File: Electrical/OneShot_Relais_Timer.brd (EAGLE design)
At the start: 65 x 63 mm, 15 parts, among them IC2 ATTINY204SOIC14, K1 RE030012, T1 BC847, X1 MKDSN1,5/3-5,08

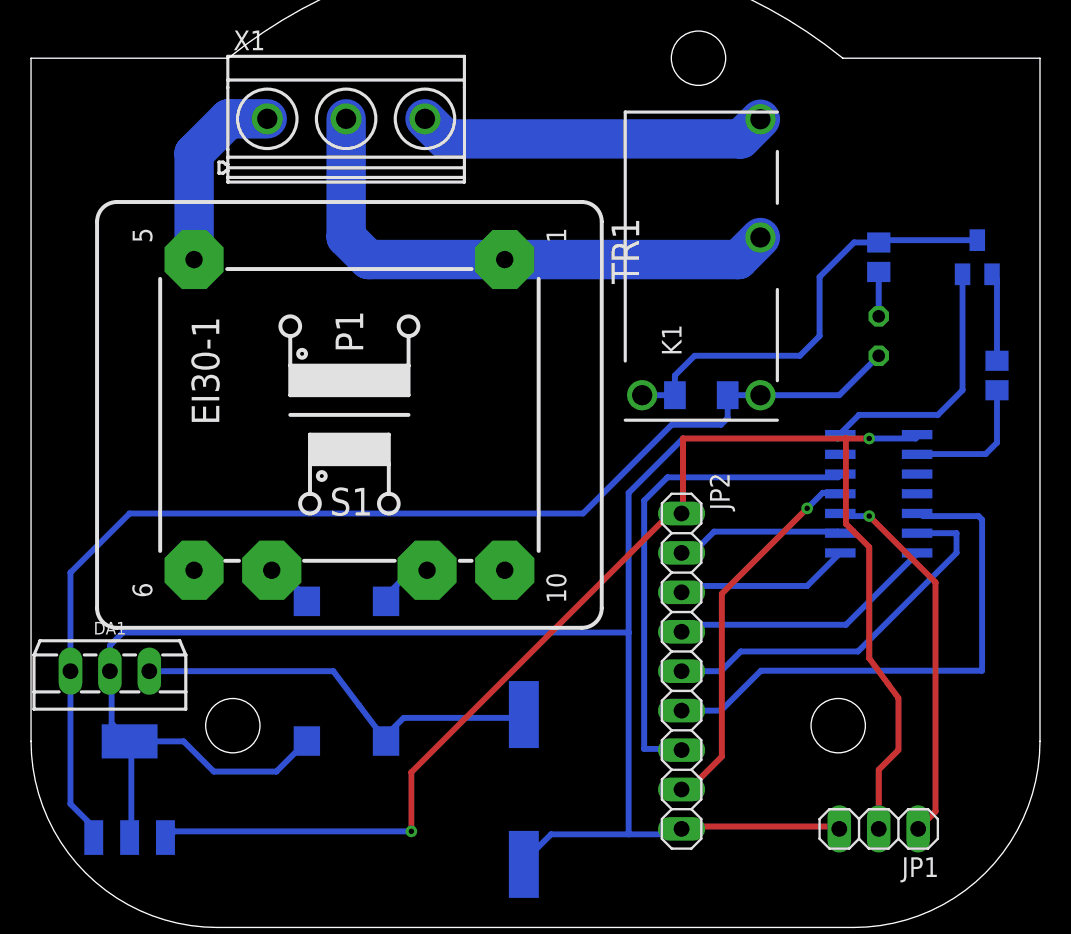
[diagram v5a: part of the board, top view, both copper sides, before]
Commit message: Added mounting hole to PCB
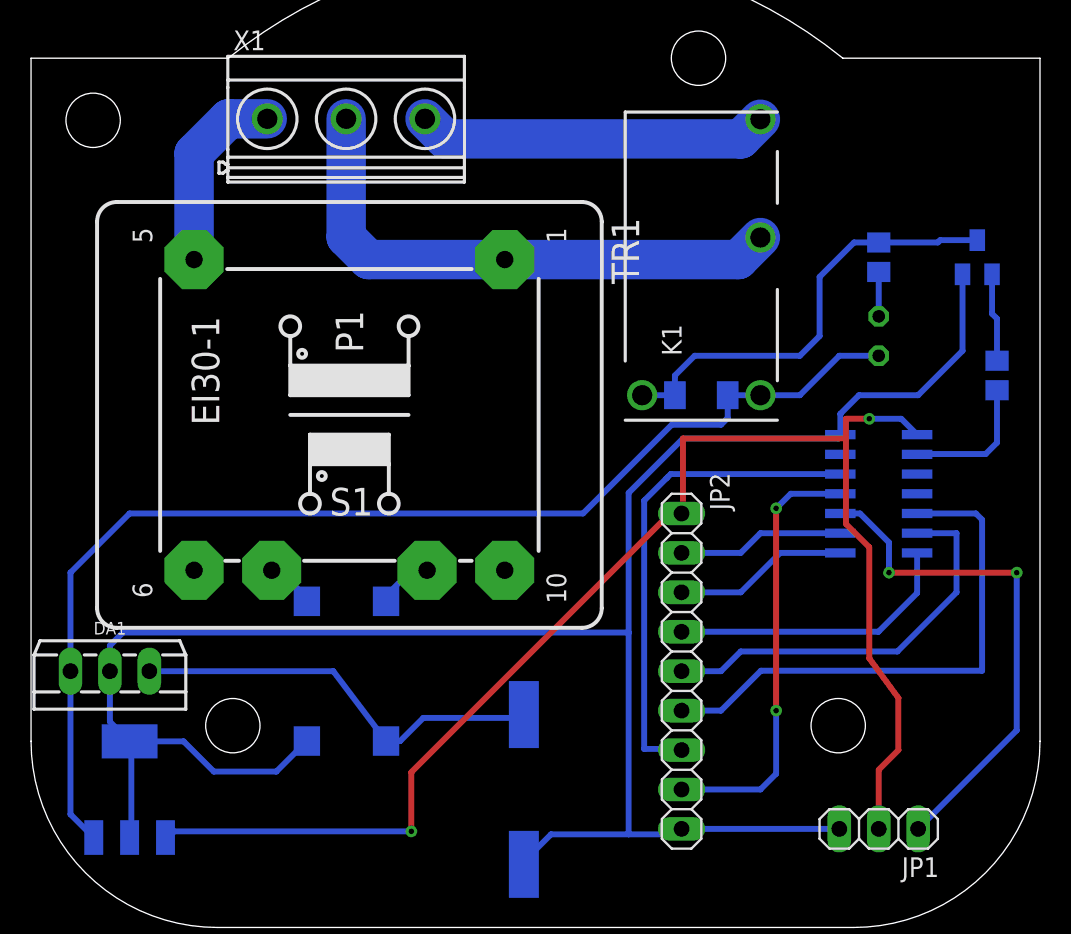
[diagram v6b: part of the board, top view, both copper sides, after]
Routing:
- net N$26: track 24.3 -> 33.2 mm, vias 1 -> 2
- net BTN_SET: track 24.8 -> 28.1 mm, vias 1 -> 2
- net +5V: track 91.1 -> 92.6 mm
- net BCD_7SEG_4: track 24.7 -> 26.2 mm
- net BCD_7SEG_3: track 17.5 -> 18.8 mm
- net GND: track 135.1 -> 134.2 mm

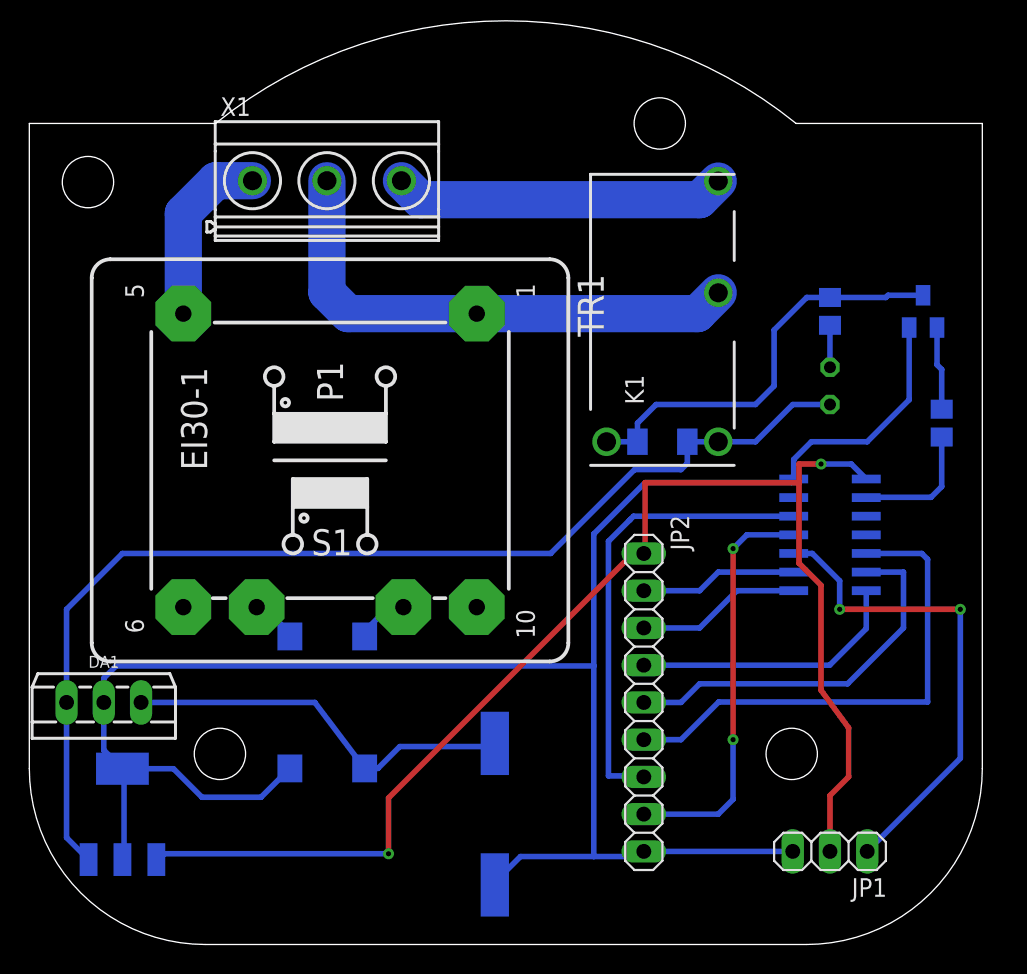
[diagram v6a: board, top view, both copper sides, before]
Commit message: Added GND planes, refined routing
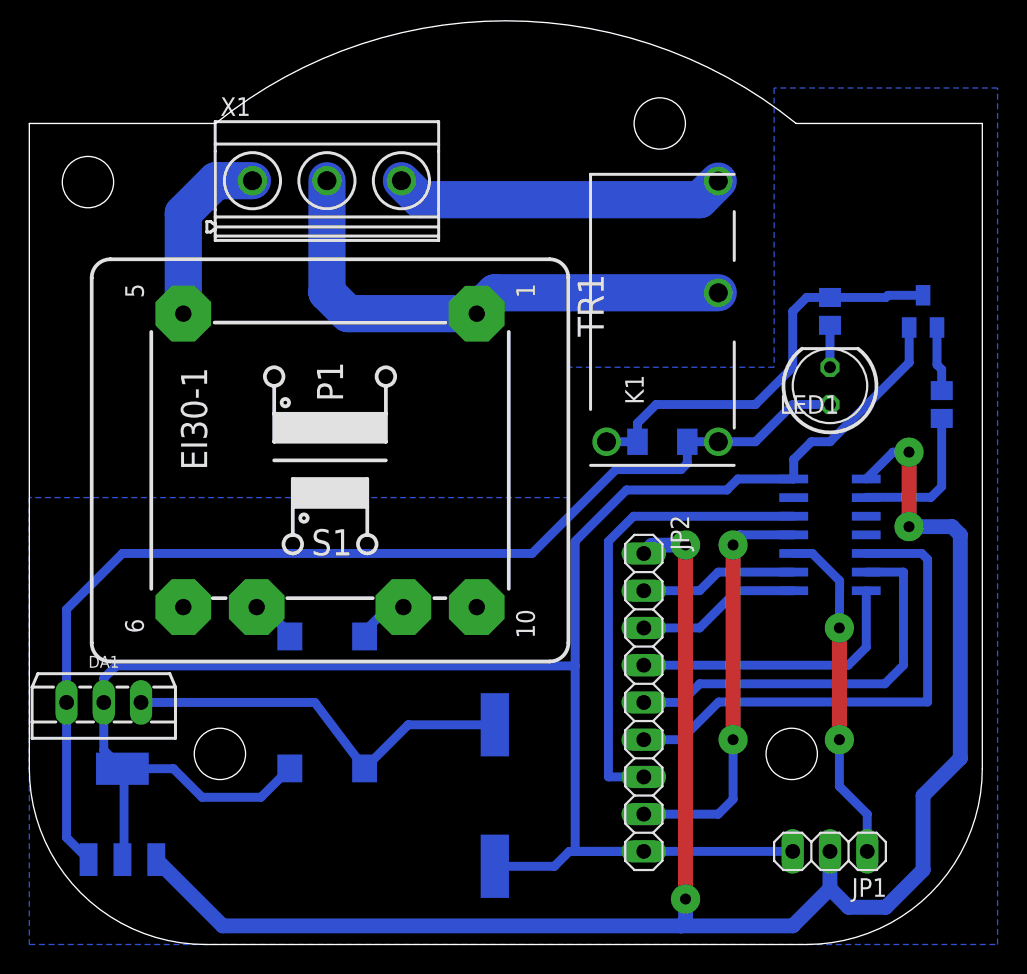
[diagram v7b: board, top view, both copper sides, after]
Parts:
- moved C1 1.27 mm to (31.8, 10.2)
- moved R1 1.27 mm to (62.2, 36.8)
- flipped LED1 to the top
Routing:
- net +5V: track 92.6 -> 124.9 mm, vias 2 -> 4
- net N$26: track 33.2 -> 23.1 mm
- net GND: track 134.2 -> 136.1 mm
- net BCD_7SEG_4: track 26.2 -> 27.7 mm
- net CTRL_RELAY: track 8.83 -> 10.1 mm
- net N$1: track 5.70 -> 4.43 mm
- net BCD_7SEG_3: track 18.8 -> 19.5 mm
- net N$21: track 27.1 -> 27.6 mm
- added copper zone on layer 16, net GND

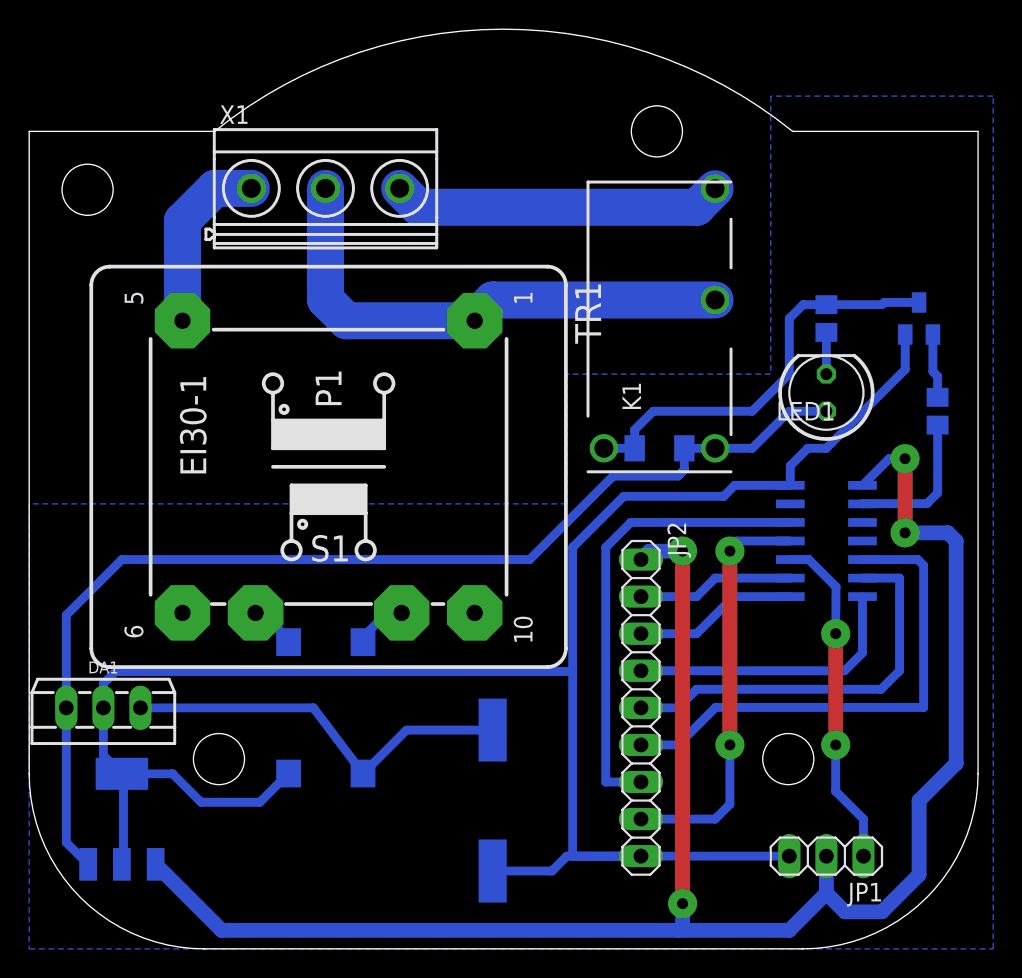
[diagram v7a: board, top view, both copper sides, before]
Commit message: Added 3D model for C1 on PCB, improved routing of PCB
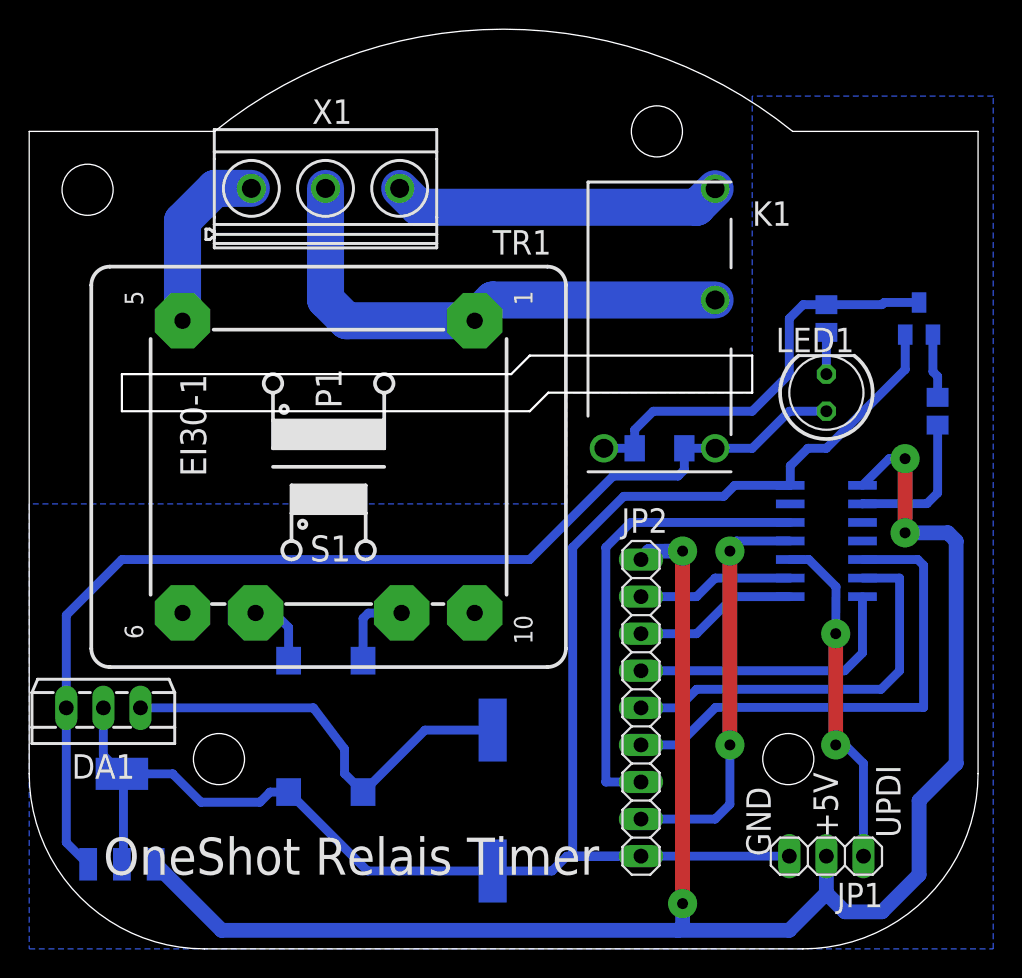
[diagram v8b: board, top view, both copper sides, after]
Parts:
- C1: device rc-master-smd:CSV-G -> OwnDevices:CSV-G
- moved B1 1.27 mm to (20.3, 15.2)
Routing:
- net GND: track 136.1 -> 117.6 mm
- net N$23: track 3.65 -> 5.70 mm
- net N$21: track 27.6 -> 29.5 mm
- net N$22: track 3.17 -> 4.95 mm
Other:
- outline, holes or cut-outs redrawn
- board text added: "+5V"
- board text added: "GND"
- board text added: "OneShot Relais Timer"
- board text added: "UPDI"
